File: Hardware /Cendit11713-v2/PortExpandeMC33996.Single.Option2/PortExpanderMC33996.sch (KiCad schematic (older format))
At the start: 11 parts, among them J1 DEBUG_CONN, P1 VIKING_HEADER_9P, P2 VIKING_HEADER_9P, U1 MC33996EKR2

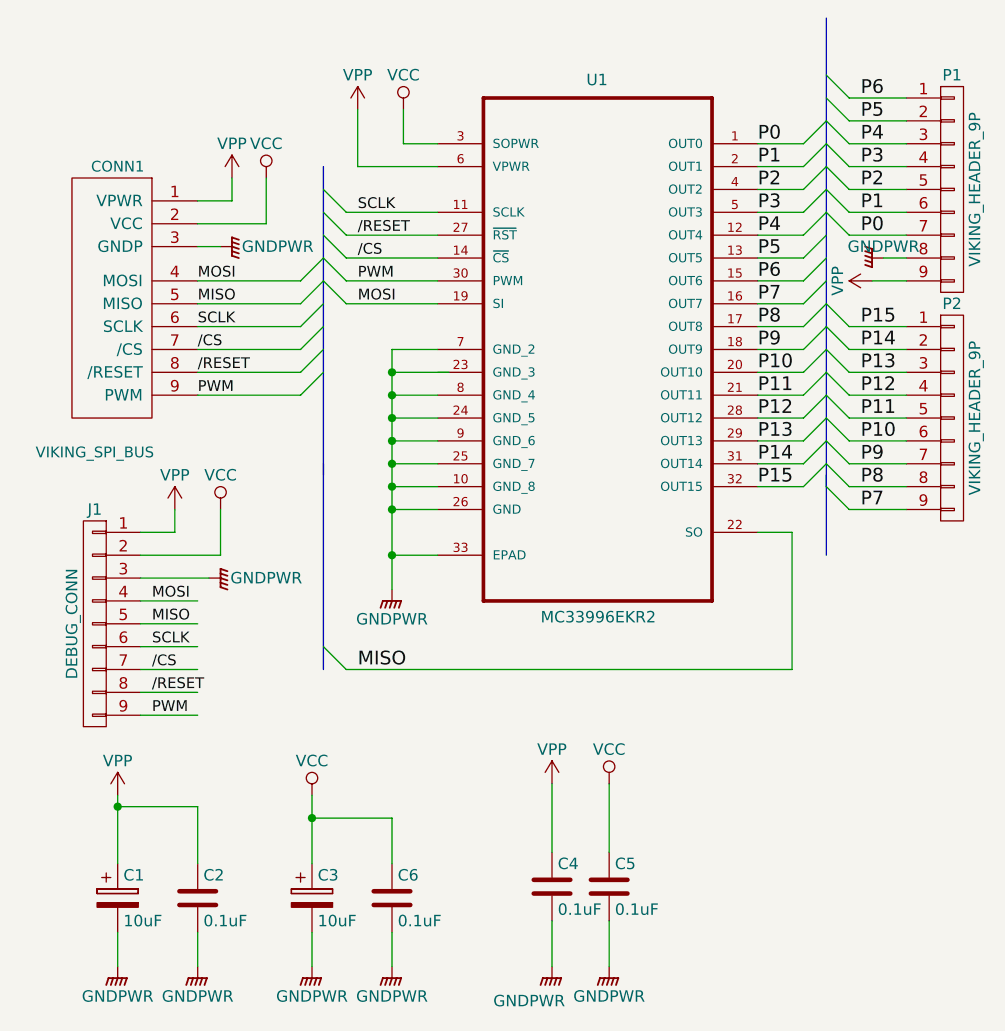
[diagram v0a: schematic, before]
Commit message: Trabajo en CenditLab + Cendit11713
  - Diseño + codigo UI
  - PCBs tarjeta madre + puertos Viking
  - Se generan Gerber para solicitud de prototipos PCB
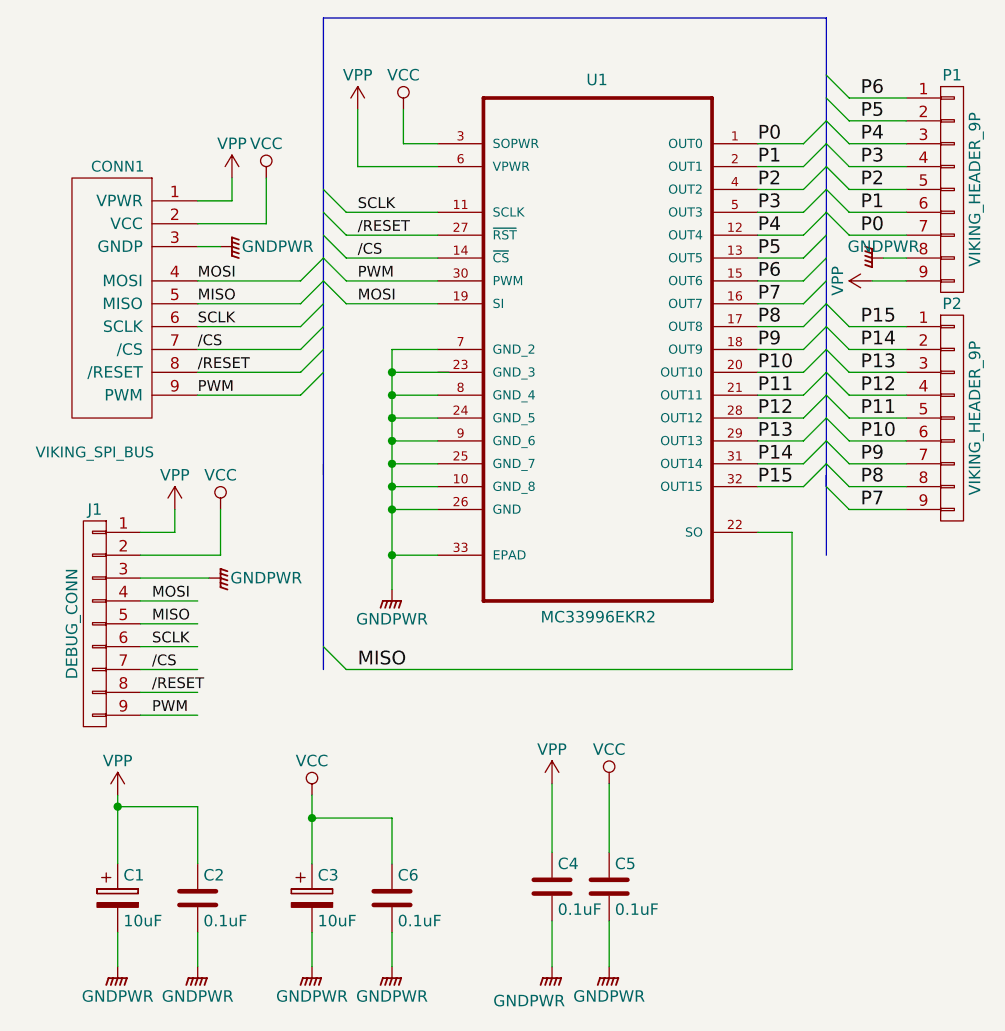
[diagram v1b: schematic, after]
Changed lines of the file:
@@
 EELAYER 25 0
 EELAYER END
-$Descr A4 11693 8268
+$Descr USLetter 11000 8500
 encoding utf-8
 Sheet 1 1
-Title ""
-Date ""
-Rev ""
-Comp ""
-Comment1 ""
-Comment2 ""
-Comment3 ""
+Title "Expansor de puertos Viking"
+Date "2017-11-23"
+Rev "Rev 1"
+Comp "CENDIT"
+Comment1 "Jose Arias"
+Comment2 "Proyecto TEG"
+Comment3 "UCV"
 Comment4 ""
 $EndDescr
@@
 $EndComp
 Wire Bus Line
-	2450 1750 2450 3100
+	2450 1100 2450 3100
 Wire Wire Line
 	2000 2100 1900 2100
@@
 	-1   0    0    -1
 $EndComp
+Wire Bus Line
+	2450 1100 4650 1100
 $EndSCHEMATC
